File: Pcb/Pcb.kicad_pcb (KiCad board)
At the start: 2 copper layers, 152.3 x 104.7 mm, 161 parts, among them J1 TRRS, Q1 2N7002, SW1 SW_Push, SW10 SW_Push, SW11 SW_Push, SW12 SW_Push, SW13 SW_Push, SW14 SW_Push, SW15 SW_Push, SW16 SW_Push, SW17 SW_Push, SW18 SW_Push, SW19 SW_Push, SW2 SW2, SW20 SW_Push, SW21 SW_Push, SW22 SW_Push, SW23 SW_Push, SW24 SW_Push, SW25 SW_Push, SW26 SW_Push, SW27 SW_Push, SW28 SW_Push, SW29 SW_Push, SW3 SW_Push, SW4 SW_Push, SW5 SW_Push, SW6 SW_Push, SW7 SW_Push, SW8 SW_Push, SW9 SW_Push, U1 ProMicro

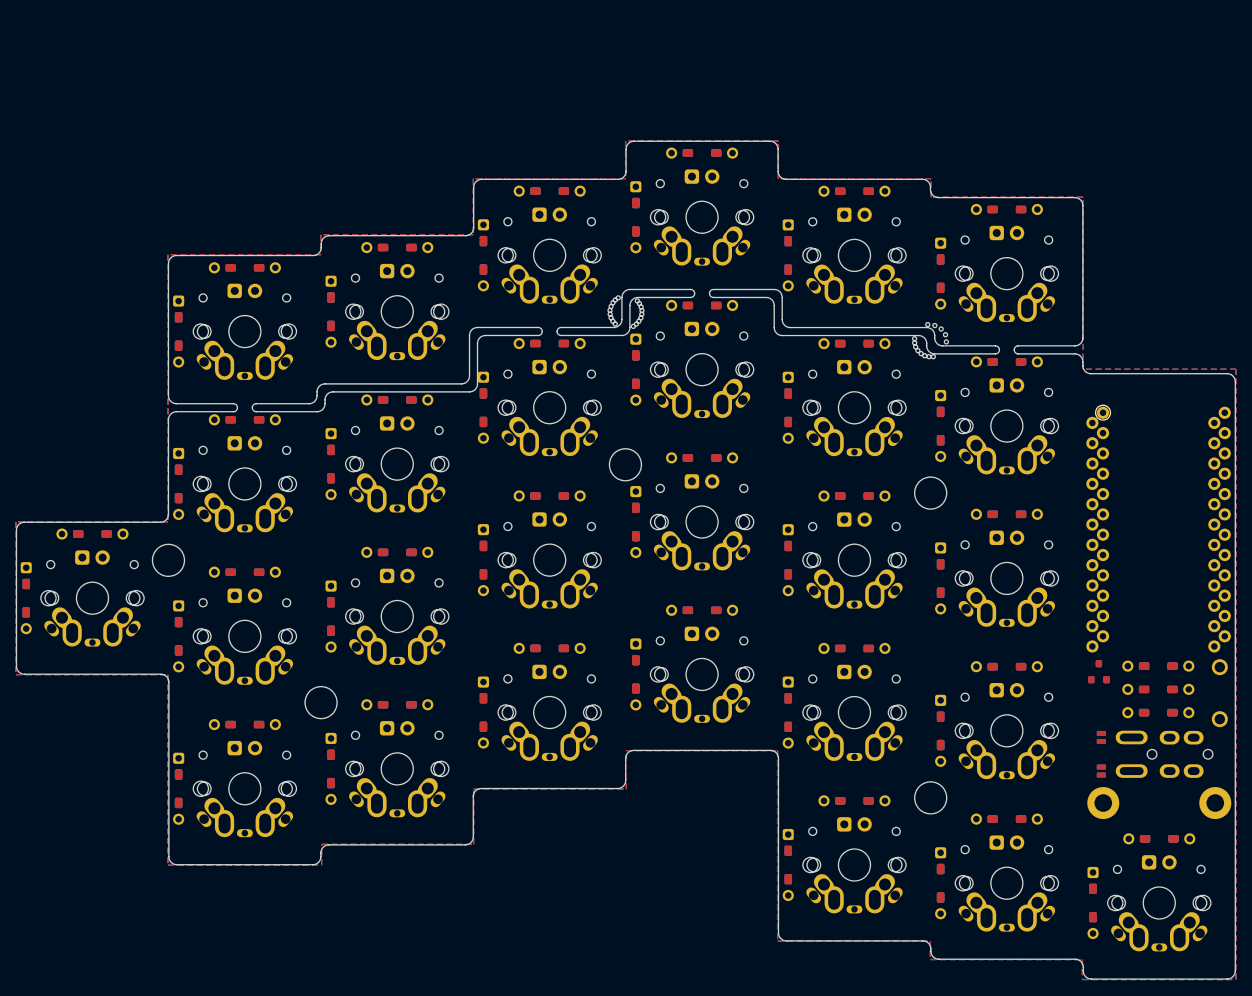
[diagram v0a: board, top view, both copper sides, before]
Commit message: Remove reference from PCB
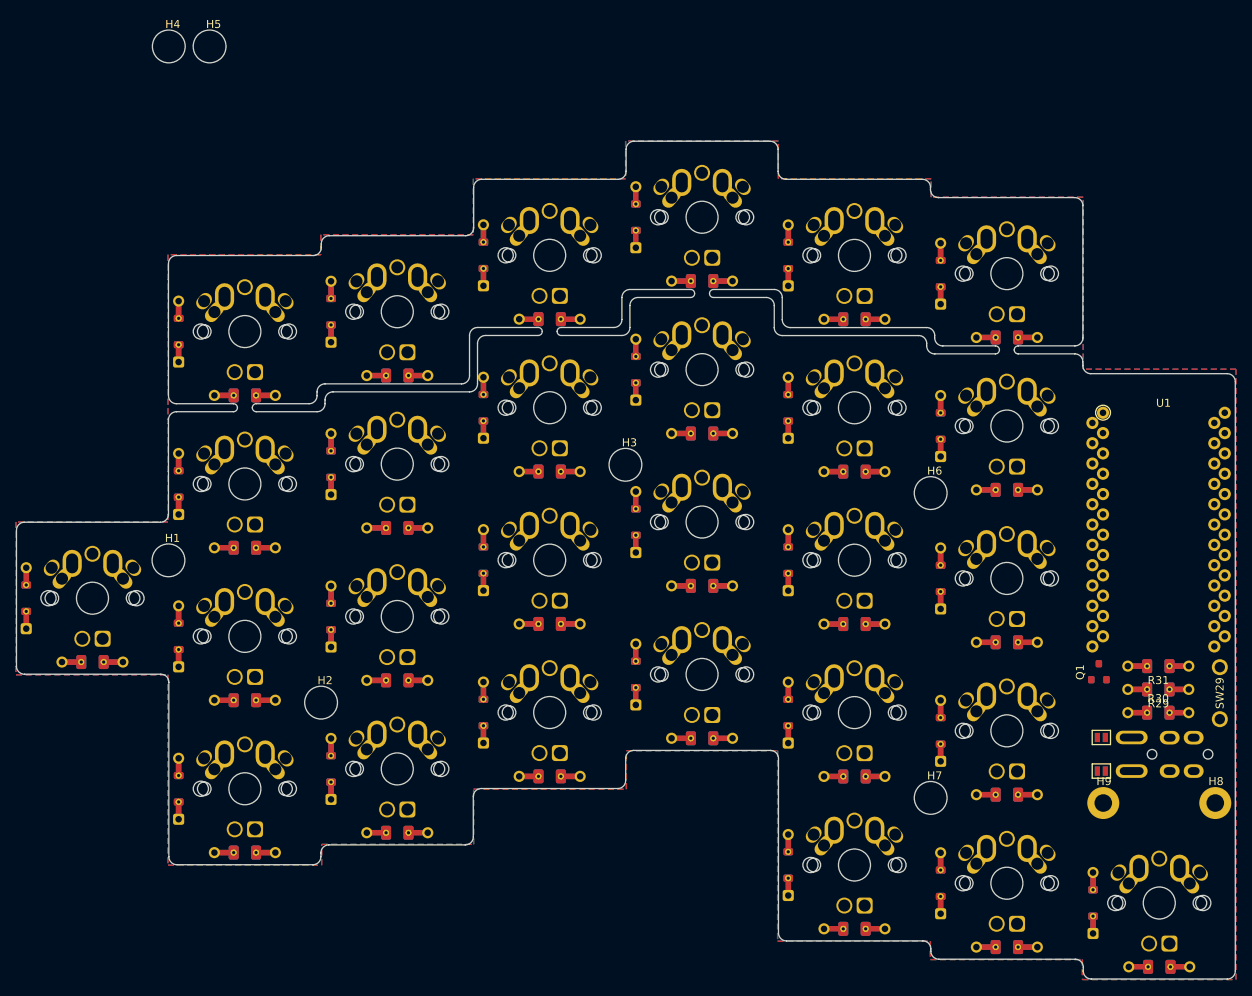
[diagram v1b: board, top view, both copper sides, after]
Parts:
- removed HB1, HB10, HB11, HB12, HB13, HB14, HB15, HB16, HB17, HB18, HB19, HB2, HB20, HB21, HB22, HB23, HB24, HB25, HB26, HB27, HB28, HB29, HB3, HB30, HB31, HB32, HB33, HB34, HB4, HB5, HB9: HoleBreak, Used_Footprints:HoleBreak
- added H4: CaseHole, Used_Footprints:Hole_Mount_M4, F.Cu at (96.2, 18.3)
- added H5: CaseHole, Used_Footprints:Hole_Mount_M4, F.Cu at (101.3, 18.3)
- D1, D10, D11, D12, D13, D14, D15, D16, D17, D18, D19, D2, D20, D21, D22, D23, D24, D25, D26, D27, D28, D3, D4, D5, D6, D7, D8, D9: footprint Used_Footprints:Diode_SMD_TH -> Used_Footprints:Diode_Hybrid_SOD-123
- D29, D30, D31, D32, D33, D34, D35, D36, D37, D38, D39, D40, D41, D42, D43, D44, D45, D46, D47, D48, D49, D50, D51, D52, D53, D54, D55, D56: footprint Used_Footprints:LED -> Used_Footprints:LED_THT_1.8mm
- H1, H2, H3, H6, H7: footprint Used_Footprints:MountHole -> Used_Footprints:Hole_Mount_M4
- H8, H9: footprint Used_Footprints:CoverHole -> Used_Footprints:Hole_Cover_M2
- J1: footprint Used_Footprints:TRSS_DUAL -> Used_Footprints:TRSS_DUAL_THT
- JP2, JP3, JP4, JP5: footprint 1kbd:jumper -> 1symblos:Jumper
- Q1: footprint Used_Footprints:SOT-23 -> Used_Footprints:Mosfet_SMD_Dual_SOT-23
- R1, R10, R11, R12, R13, R14, R15, R16, R18, R19, R2, R20, R21, R22, R23, R24, R25, R26, R27, R28, R29, R3, R30, R31, R4, R5, R6, R7, R8, R9: footprint Used_Footprints:Resistor_SMD_TH -> Used_Footprints:Resistor_Hybrid_1205
- R17: value R_Small -> e; footprint Used_Footprints:Resistor_SMD_TH -> Used_Footprints:Resistor_Hybrid_1205
- SW1, SW10, SW11, SW12, SW13, SW14, SW15, SW16, SW17, SW18, SW19, SW2, SW20, SW21, SW22, SW23, SW24, SW25, SW26, SW27, SW28, SW3, SW4, SW5, SW6, SW7, SW8, SW9: footprint 1symblos:cherry -> Used_Footprints:Switch_MxAlpsChoc_MillMax_1u
- SW29: footprint Used_Footprints:Reset_Switch -> Used_Footprints:Switch_Reset_THT
- U1: footprint Used_Footprints:ProMicro_TwoSide -> Used_Footprints:ProMicro_Dual
- moved R9 16.0 mm to (143.8, 71.4), turned to 0 degrees
- moved R4 16.0 mm to (162.9, 47.6), turned to 0 degrees
- moved R10 16.0 mm to (162.9, 66.6), turned to 0 degrees
- moved R11 16.0 mm to (181.9, 71.4), turned to 0 degrees
- moved R12 16.0 mm to (201.0, 73.7), turned to 0 degrees
- moved R13 16.0 mm to (105.7, 100.0), turned to 0 degrees
- moved R14 16.0 mm to (124.8, 97.5), turned to 0 degrees
- moved R15 16.0 mm to (143.8, 90.5), turned to 0 degrees
- moved R16 16.0 mm to (162.9, 85.7), turned to 0 degrees
- moved R17 16.0 mm to (181.9, 90.5), turned to 0 degrees
- moved R18 16.0 mm to (201.0, 92.7), turned to 0 degrees
- moved R19 16.0 mm to (105.7, 119.0), turned to 0 degrees
- moved R2 16.0 mm to (124.8, 59.4), turned to 0 degrees
- moved R20 16.0 mm to (124.8, 116.5), turned to 0 degrees
- moved R21 16.0 mm to (143.8, 109.5), turned to 0 degrees
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
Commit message: Add one more mount hole
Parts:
- removed H3, H4, H5, H6, H7: CaseHole, Used_Footprints:Hole_Mount_M4
- removed H8, H9: CoverHole, Used_Footprints:Hole_Cover_M2
- added HC1: CoverHole, Used_Footprints:Hole_Cover_M2, F.Cu at (250.6, 70.8)
- added HC2: CoverHole, Used_Footprints:Hole_Cover_M2, F.Cu at (255.6, 70.8)
- added HM3: CaseHole, Used_Footprints:Hole_Mount_M4, F.Cu at (191.4, 55.0)
- added HM4: CaseHole, Used_Footprints:Hole_Mount_M4, F.Cu at (153.3, 51.5)
- added HM5: CaseHole, Used_Footprints:Hole_Mount_M4, F.Cu at (153.3, 70.6)
- added HM6: CaseHole, Used_Footprints:Hole_Mount_M4, F.Cu at (115.2, 81.2)
- added HM7: CaseHole, Used_Footprints:Hole_Mount_M4, F.Cu at (115.2, 100.3)
- added HM8: CaseHole, Used_Footprints:Hole_Mount_M4, F.Cu at (96.2, 82.5)
- R17: value e -> R_Small
- moved HM1 99.8 mm to (191.4, 112.2)
- moved HM2 80.6 mm to (191.4, 74.1)
- renumbered H1 to HM1, H2 to HM2

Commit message: Remove case silkscreen
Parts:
- moved HC1 56.4 mm to (213.0, 112.8)
- moved HC2 50.8 mm to (227.0, 112.8)

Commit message: Remove outline zone
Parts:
- turned JP2 to 270 degrees
- turned JP3 to 90 degrees
- turned JP4 to 270 degrees
- turned JP5 to 90 degrees
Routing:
- removed copper zone on B.Cu, net (none)
- removed copper zone on F.Cu, net (none)
